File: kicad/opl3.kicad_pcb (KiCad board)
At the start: 2 copper layers, 52.1 x 35.6 mm, 46 parts, among them J1 Conn_01x08, J2 AudioJack2_Ground_Switch, U1 YMF262, U2 YAC512, U3 LM2902, U4 NE5532, U5 74HC595, U6 SN74LVC1G14DBV, X1 14.318MHz

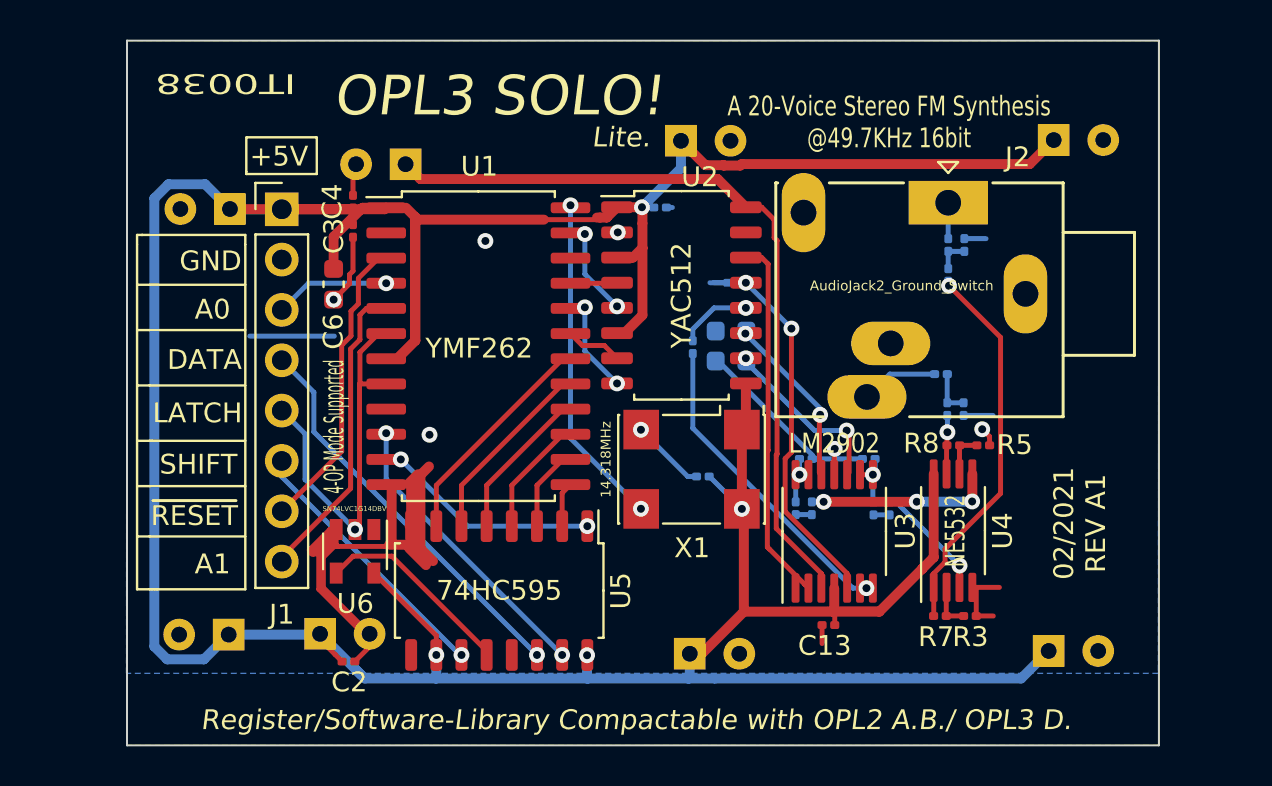
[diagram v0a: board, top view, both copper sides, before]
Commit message: A add on module enables ALL opl3's channel.
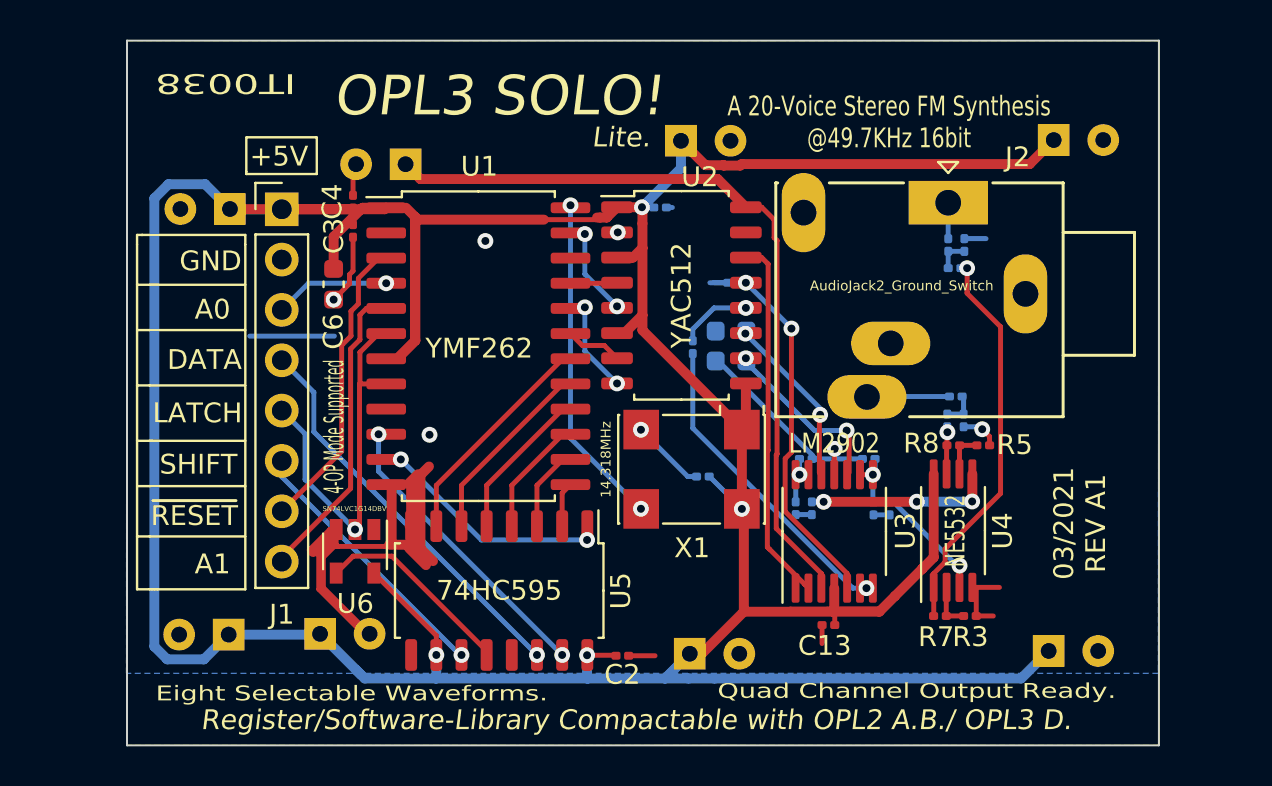
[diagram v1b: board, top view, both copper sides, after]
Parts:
- moved C2 13.8 mm to (149.4, 119.1)
- moved R10 1.36 mm to (166.2, 106.0)
- moved C22 0.57 mm to (165.7, 107.3)
- moved R22 0.57 mm to (166.6, 107.3)
- moved C21 0.47 mm to (166.1, 99.6), turned to 0 degrees
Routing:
- net +5V: track 211.9 -> 219.7 mm
- net Net-(J2-PadR): track 3.89 -> 5.01 mm
- net GND: track 71.2 -> 70.3 mm
- net Net-(C22-Pad2): track 2.97 -> 2.12 mm
- net Net-(C22-Pad1): track 2.27 -> 1.76 mm
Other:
- board text added: "03/2021 REV A1"
- board text added: "Eight Selectable Waveforms."
- board text added: "Quad Channel Output Ready."
- board text removed: "02/2021 REV A1"
